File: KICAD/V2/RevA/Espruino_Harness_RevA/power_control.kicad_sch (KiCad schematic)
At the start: 18 parts, among them J1001 OPERATING_MODE, Q1001 2N7002, U1001 TPS2116DRL, U1002 TPS22917DBV

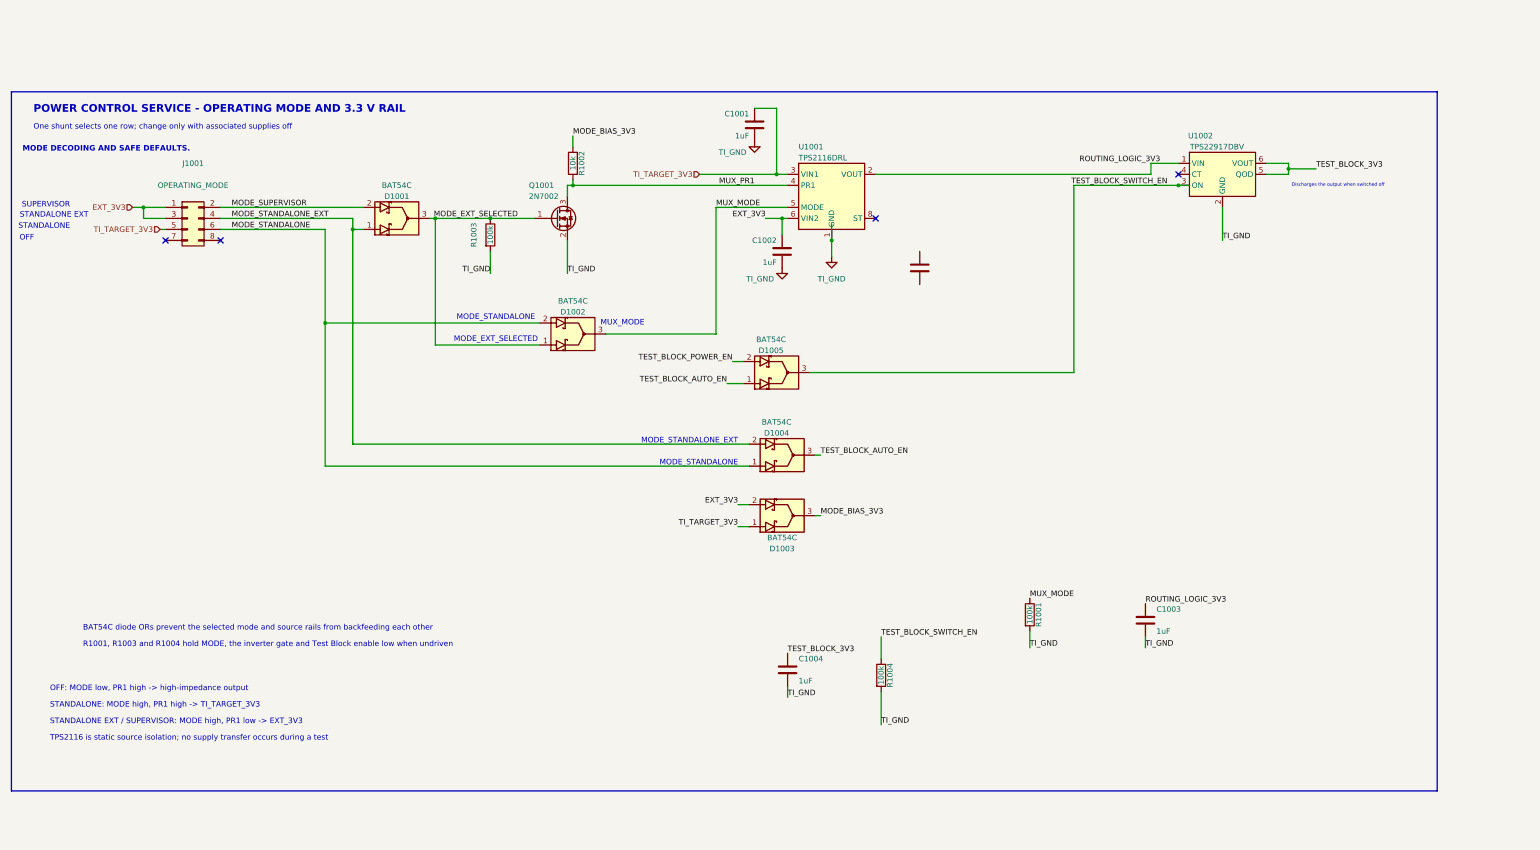
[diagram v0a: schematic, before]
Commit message: Integrate Rev-A power control and rack supply requirements
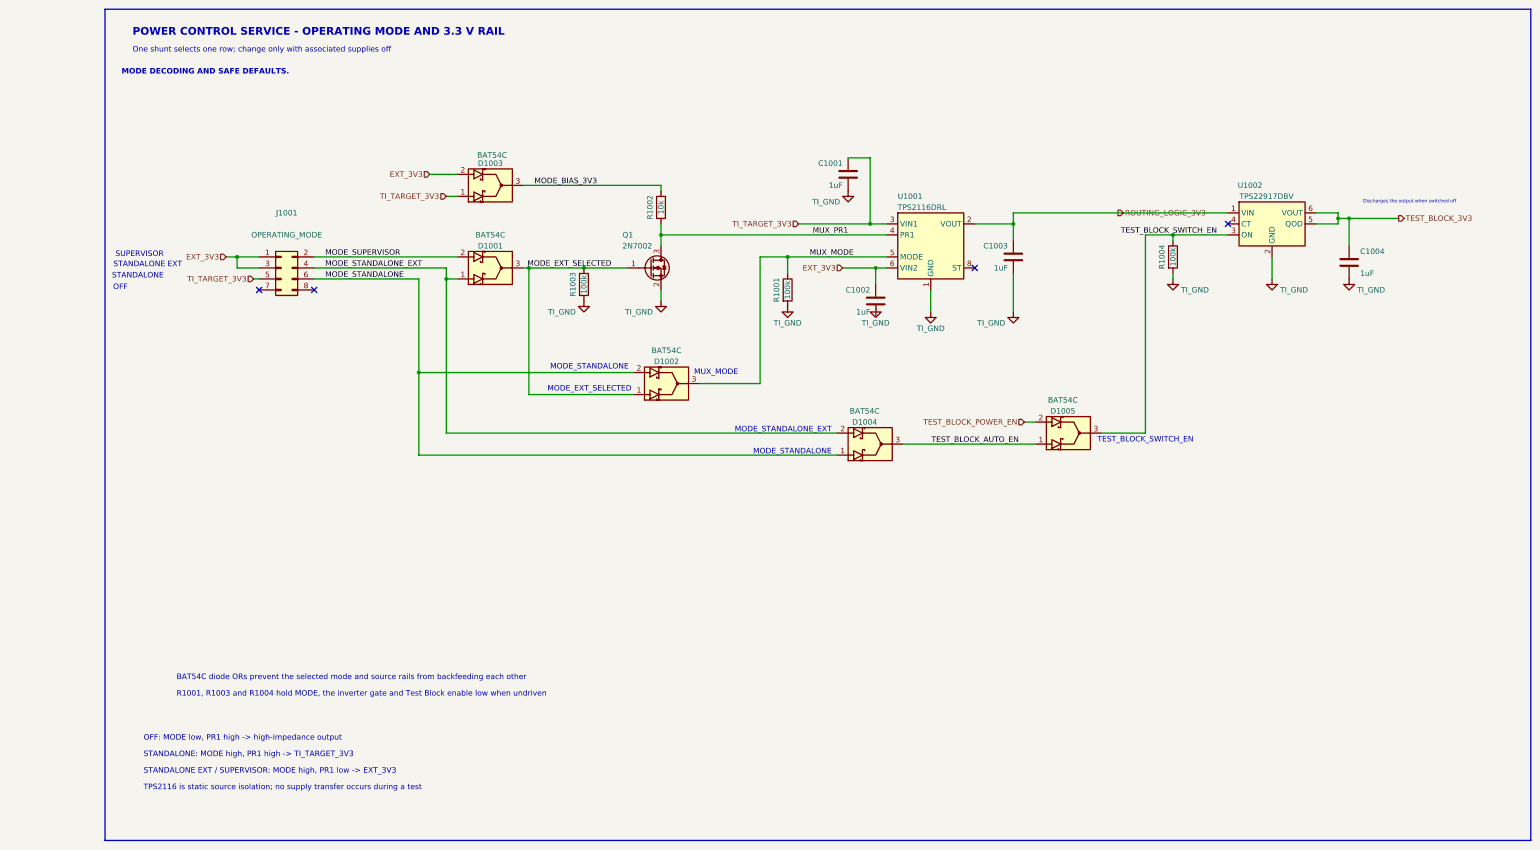
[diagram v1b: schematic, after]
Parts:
- removed C1002, C1003: 1uF, Capacitor_SMD:C_0603_1608Metric, symbol Device:C
- added C1003: 1uF, Capacitor_SMD:C_0603_1608Metric, symbol Espruino_Harness_RevA:C
- C1001, C1002: symbol Device:C -> Espruino_Harness_RevA:C
- J1001: symbol Connector_Generic:Conn_02x04_Odd_Even -> Espruino_Harness_RevA:Operating_Mode_2x04
- R1001, R1002, R1003: symbol Device:R -> Espruino_Harness_RevA:R
- U1001: symbol Power_Management:TPS2116DRL -> Espruino_Harness_RevA:TPS2116DRL_POWER_MUX
- U1002: symbol Power_Management:TPS22917DBV -> Espruino_Harness_RevA:TPS22917DBV_LOAD_SWITCH
- renumbered Q1001 to Q1
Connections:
- net ROUTING_LOGIC_3V3: now also U1001.2 (VOUT), U1001.7 (VOUT), U1002.1 (VIN), C1003.2
- net TI_GND: now also C1003.1
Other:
- note added: "TEST_BLOCK_SWITCH_EN"
- company: ESP32_SGATest -> SimonGAndrews
- title: DRAFT WORKBENCH - NOT IN PRODUCTION HIERARCHY -> V2 Rev-A Power Control Service
- moved on the sheet: C1001, C1002, C1004, D1001, D1002, D1003, D1004, D1005, J1001, Q1, R1001, R1002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

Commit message: Establish Rev-A schematic verification framework
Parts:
- added C1101: 1uF, Capacitor_SMD:C_0603_1608Metric, symbol Espruino_Harness_RevA:C
- added C1102, C1103, C1104, C1105, C1106: 100nF, Capacitor_SMD:C_0603_1608Metric, symbol Espruino_Harness_RevA:C
- added Q1101: AO3401A, Package_TO_SOT_SMD:SOT-23, symbol Espruino_Harness_RevA:AO3401A_LOW_RANGE_BYPASS
- added R1009, R1103, R1104, R1106, R1107, R1110: 100k, Resistor_SMD:R_0603_1608Metric, symbol Espruino_Harness_RevA:R
- added R1101: 0.050R 0.1%, Resistor_SMD:R_0603_1608Metric, symbol Espruino_Harness_RevA:R
- added R1102: 1.00R 0.1%, Resistor_SMD:R_0603_1608Metric, symbol Espruino_Harness_RevA:R
- added R1105, R1108, R1112: 10k, Resistor_SMD:R_0603_1608Metric, symbol Espruino_Harness_RevA:R
- added R1111: 66.5k 1%, Resistor_SMD:R_0603_1608Metric, symbol Espruino_Harness_RevA:R
- added U1101: TPS2559-Q1, symbol Espruino_Harness_RevA:TPS2559Q1_TARGET_POWER_SWITCH
- added U1102: 74AHCT1G125, Package_TO_SOT_SMD:SOT-23-5, symbol Espruino_Harness_RevA:74AHCT1G125_RANGE_DRIVER
- added U1103: INA226, Package_SO:VSSOP-10_3x3mm_P0.5mm, symbol Espruino_Harness_RevA:INA226_HIGH_RANGE
- added U1104: INA228, Package_SO:VSSOP-10_3x3mm_P0.5mm, symbol Espruino_Harness_RevA:INA228_LOW_RANGE
- added U1105: 74LVC2G08, Package_SO:VSSOP-8_2.3x2mm_P0.5mm, symbol Espruino_Harness_RevA:74LVC2G08_POWER_CONTROL
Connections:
- net MODE_SUPERVISOR: now also R1009.1, U1105.1 (1A)
- net TI_GND: now also C1101.2, C1102.2, C1103.2, C1104.2, C1105.2, C1106.2, R1009.2, R1103.2, R1104.2, R1106.2, R1107.2, R1110.2, R1111.2, U1101.1 (GND), U1101.11 (PowerPAD), U1102.1 (~{OE}), U1102.3 (GND), U1103.1 (A1), U1103.2 (A0), U1103.7 (GND), U1104.1 (A1), U1104.7 (GND), U1105.4 (GND)
- new net EXT_5V: C1101.1, C1106.1, U1101.2 (IN), U1101.3 (IN), U1101.4 (IN), U1102.5 (VCC)
- new net HIGH_SHUNT_N: Q1101.2 (S), R1101.2, R1102.1, U1103.9 (Vin-), U1104.10 (Vin+)
- new net HIGH_SHUNT_P: C1102.1, R1101.1, U1101.7 (OUT), U1101.8 (OUT), U1101.9 (OUT), U1103.10 (Vin+)
- new net LOW_RANGE_GATE_3V3: R1106.1, U1102.2 (A), U1105.3 (2Y)
- new net LOW_RANGE_OK_N: R1105.2, U1104.3 (~{Alert}), U1105.6 (2B)
- new net LOW_SHUNT_BYPASS_GATE: Q1101.1 (G), R1107.1, U1102.4 (Y)
- new net RACK_CONTROL_3V3: C1103.1, C1104.1, C1105.1, R1105.1, R1108.1, R1112.1, U1103.6 (VS), U1104.2 (A0), U1104.6 (VS), U1105.8 (VCC)
- new net RACK_CONTROL_SCL: U1103.5 (SCL), U1104.5 (SCL)
- new net RACK_CONTROL_SDA: U1103.4 (SDA), U1104.4 (SDA)
- new net TARGET_CURRENT_LIMIT_SET: R1111.1, U1101.6 (ILIM)
- new net TARGET_LOW_RANGE_EN: R1104.1, U1105.5 (2A)
- new net TARGET_POWER_ALERT_N: R1108.2, U1103.3 (~{Alert})
- new net TARGET_POWER_EN: R1103.1, U1105.2 (1B)
- new net TARGET_POWER_FAULT_N: R1112.2, U1101.10 (FAULT)
- new net TARGET_SWITCH_EN: R1110.1, U1101.5 (EN), U1105.7 (1Y)
- new net TI_SWITCHED_TARGET_5V: Q1101.3 (D), R1102.2, U1103.8 (Vbus), U1104.8 (Vbus), U1104.9 (Vin-)
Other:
- note added: "Firmware sequence: confirm current below threshold -> select low range -> measure sleep -> restore normal range before wake/reset."
- note added: "HIGH_SHUNT_N"
- note added: "Kelvin sense routing required directly from each shunt pad to its corresponding monitor IN+/IN− pins"
- note added: "LOW RANGE: INA228 at 0x41; 1 ohm, 0.1%, low-TCR shunt"
- note added: "LOW_RANGE_GATE_3V3 = TARGET_LOW_RANGE_EN AND LOW_RANGE_OK_N"
- note added: "NORMAL RANGE: INA226 at 0x40; 50 mOhm, 0.1%, low-TCR shunt"
- note added: "Q1101 bypasses R1102 by default. Low-range request opens the bypass; INA228 ALERT immediately restores the bypass on over-current"
- note added: "Selects address 0x40"
- note added: "Selects address 0x41"
- note added: "Supervisor-only power path; high-current range is the hardware-safe default"
- note added: "TARGET 5 V SWITCH AND TWO-RANGE POWER MONITOR"
- note added: "TARGET_SWITCH_EN = MODE_SUPERVISOR AND TARGET_POWER_EN"
- note added: "TPS22963C provides controlled turn-on and reverse-current protection while off. No output discharge: Standalone USB power must not be loaded by the harness switch. Verify DSBGA assembly availability with AISLER."
- moved on the sheet: C1001, C1002, C1003, C1004, D1001, D1002, D1003, D1004, D1005, J1001, Q1, R1001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

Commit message: Integrate Rev-A rack control endpoint
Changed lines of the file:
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@@
+	(wire
+		(pts
+			(xy 251.46 86.36) (xy 257.81 86.36)
+		)
+		(stroke
+			(width 0)
+			(type default)
+		)
+	)
 	(wire
 		(pts
@@
 	(wire
 		(pts
-			(xy 257.81 92.71) (xy 255.27 92.71)
-		)
-		(stroke
-			(width 0)
-			(type default)
-		)
-	)
-	(wire
-		(pts
 			(xy 171.45 38.1) (xy 171.45 39.37)
 		)
@@
 		(pts
 			(xy 139.7 38.1) (xy 171.45 38.1)
+		)
+		(stroke
+			(width 0)
+			(type default)
+		)
+	)
+	(wire
+		(pts
+			(xy 257.81 86.36) (xy 257.81 92.71)
 		)
 		(stroke
@@
 	(hierarchical_label "TEST_BLOCK_POWER_EN"
 		(shape input)
-		(at 255.27 92.71 180)
-		(effects
-			(font
+		(at 251.46 86.36 180)
+		(effects
+			(font
